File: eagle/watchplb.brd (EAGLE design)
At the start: 100 x 80 mm, 53 parts, among them IC1 SAM-M8Q, IC2 BM70BLES1FC2-0B03AA, Q1 8MHz / LFXTAL020423Reel, U1 MCP111-XXXXX/TO, U2 STM32L073RZ, U3 MCP2200-I/SS

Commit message: update
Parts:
- added C19: CSTCE12M0G15L99-R0, 12mhz osc:CSTCE
- added C20: 1uF, resistor:C0805
- added D1: S8NC-13, diode:SMC
- added J1: (no value), SparkFun-Connectors:USB-B-MICRO-SMD
- added JP2: VIB_MOTOR, 619-28821, pinhead:1X02
- added LED10: YELLOW, adafruit:CHIP-LED0805
- added LED11, LED6, LED7, LED8: GREEN, adafruit:CHIP-LED0805
- added LED12, LED9: RED, adafruit:CHIP-LED0805
- added Q2: DMT5015LFDF, Hick:U-DFN2020-6_TYPE_F
- added R18, R19, R20, R21, R22, R23, R24: 220R, resistor:M0805
- added R25: 100k, resistor:M0805
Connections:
- net N$10 renamed IND_LED_B
- net N$15 renamed IND_LED_W
- net N$17 renamed IND_LED_R
- net N$8 renamed IND_LED_G
- removed net VDD: U3.1
- removed net VSS: U3.20
- removed net VUSB: U3.17
- new net +5V: J1.VBUS, U3.1
- new net N$10: C19.3, U3.3
- new net N$13: LED9.A, R21.2
- new net N$15: C19.1, U3.2
- new net N$17: J1.D-, U3.18
- new net N$19: LED6.A, R18.2
- new net N$20: J1.D+, U3.19
- new net N$21: C20.1, U3.17
- new net N$22: LED7.A, R19.2
- new net N$23: LED12.A, R24.2
- new net N$24: LED10.A, R22.2
- new net N$25: LED8.A, R20.2
- new net N$26: LED11.C, U3.6
- new net N$27: LED12.C, U3.5
- new net N$28: D1.A, JP2.2, Q2.1, Q2.2, Q2.5, Q2.6, Q2.7
- new net N$8: LED11.A, R23.2
- new net POW_LED_G1: R20.1, U2.24
- new net POW_LED_G2: R19.1, U2.25
- new net POW_LED_G3: R18.1, U2.26
- new net POW_LED_R: R21.1, U2.22
- new net POW_LED_Y: R22.1, U2.23
- new net SWD_RX: U3.12
- new net SWD_RXD: U2.16
- new net SWD_TX: U3.10
- new net SWD_TXD: U2.17
- new net V+: D1.C, JP2.1
- new net VIBRATOR: Q2.3, R25.1, U2.44
- net +3V3: now also R23.1, R24.1, U3.4
- net GND: now also C19.2, C20.2, J1.GND, J1.SHIELD1, J1.SHIELD2, J1.SHIELD3, LED10.C, LED6.C, LED7.C, LED8.C, LED9.C, Q2.4, Q2.8, R25.2, U3.20
- net GPS_RXD: now also U2.51; no longer U2.16
- net GPS_TXD: now also U2.52; no longer U2.17

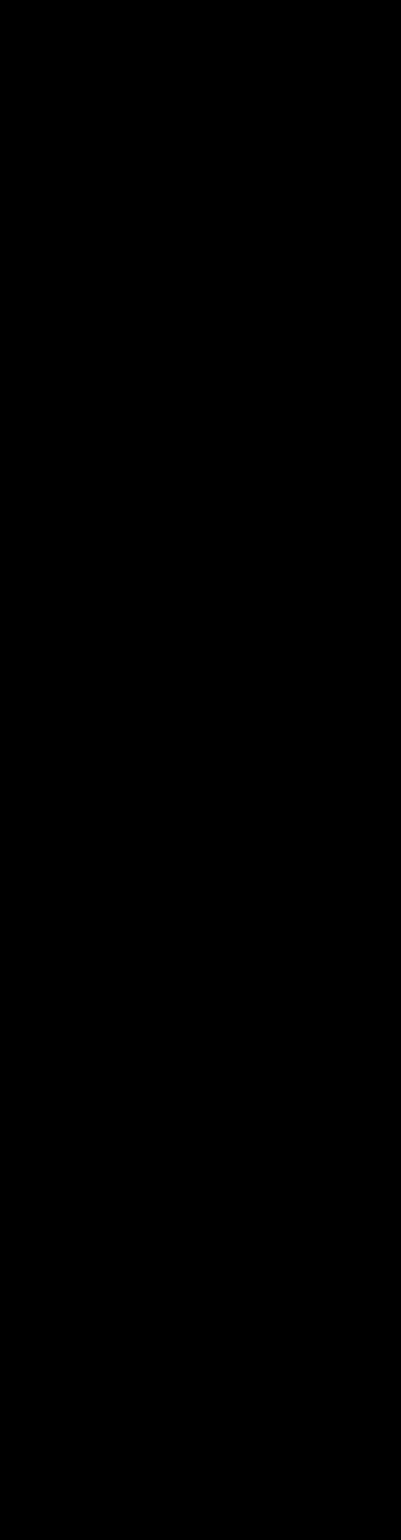
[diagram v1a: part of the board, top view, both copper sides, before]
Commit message: added testpoints, moved pins so pb11 is free to make it pin kompatibel to another prozessor with more power
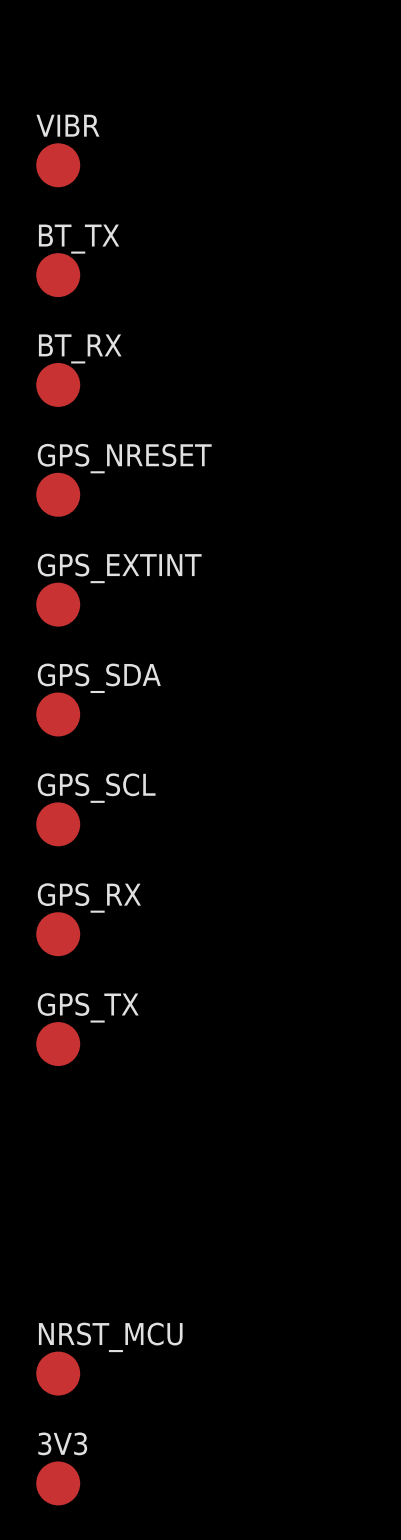
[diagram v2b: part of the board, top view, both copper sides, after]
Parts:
- added 3V3, BT_RX, BT_TX, GPS_EXTINT, GPS_NRESET, GPS_RX, GPS_SCL, GPS_SDA, GPS_TX, NRST_MCU, VIBR: PTR1B2,54, testpad:B2,54
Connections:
- new net RESERVED: U2.30
- net +3V3: now also 3V3.TP
- net BT_HCI_RXD: now also BT_RX.TP
- net BT_HCI_TXD: now also BT_TX.TP
- net GPS_EXTINT: now also GPS_EXTINT.TP
- net GPS_NRESET: now also GPS_NRESET.TP
- net GPS_RXD: now also GPS_RX.TP
- net GPS_SCL: now also GPS_SCL.TP
- net GPS_SDA: now also GPS_SDA.TP
- net GPS_TXD: now also GPS_TX.TP
- net IND_LED_B: now also U2.27; no longer U2.29
- net IND_LED_G: now also U2.28; no longer U2.30
- net IND_LED_R: now also U2.25; no longer U2.27
- net IND_LED_W: now also U2.26; no longer U2.28
- net NRST: now also NRST_MCU.TP
- net POW_LED_G1: now also U2.22; no longer U2.24
- net POW_LED_G2: now also U2.23; no longer U2.25
- net POW_LED_G3: now also U2.24; no longer U2.26
- net POW_LED_R: now also U2.20; no longer U2.22
- net POW_LED_Y: now also U2.21; no longer U2.23
- net VIBRATOR: now also VIBR.TP

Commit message: no message
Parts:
- added SWD_RXD, SWD_TXD, USB_5V, USB_D+, USB_D-: PTR1B2,54, testpad:B2,54
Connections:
- net +5V: now also USB_5V.TP
- net N$17: now also USB_D-.TP
- net N$20: now also USB_D+.TP
- net SWD_RXD: now also SWD_RXD.TP
- net SWD_TXD: now also SWD_TXD.TP
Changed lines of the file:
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@@
 <attribute name="TP_SIGNAL_NAME" value="" x="-121.92" y="-521.97" size="1.778" layer="27" display="off"/>
+</element>
+<element name="USB_D-" library="testpad" package="B2,54" value="PTR1B2,54" x="-121.92" y="-528.32">
+<attribute name="TP_SIGNAL_NAME" value="" x="-121.92" y="-528.32" size="1.778" layer="27" display="off"/>
+</element>
+<element name="USB_D+" library="testpad" package="B2,54" value="PTR1B2,54" x="-121.92" y="-534.67">
+<attribute name="TP_SIGNAL_NAME" value="" x="-121.92" y="-534.67" size="1.778" layer="27" display="off"/>
+</element>
+<element name="USB_5V" library="testpad" package="B2,54" value="PTR1B2,54" x="-121.92" y="-541.02">
+<attribute name="TP_SIGNAL_NAME" value="" x="-121.92" y="-541.02" size="1.778" layer="27" display="off"/>
+</element>
+<element name="SWD_TXD" library="testpad" package="B2,54" value="PTR1B2,54" x="-121.92" y="-547.37">
+<attribute name="TP_SIGNAL_NAME" value="" x="-121.92" y="-547.37" size="1.778" layer="27" display="off"/>
+</element>
+<element name="SWD_RXD" library="testpad" package="B2,54" value="PTR1B2,54" x="-121.92" y="-553.72">
+<attribute name="TP_SIGNAL_NAME" value="" x="-121.92" y="-553.72" size="1.778" layer="27" display="off"/>
 </element>
 </elements>
@@
 <contactref element="J1" pad="D-"/>
 <contactref element="U3" pad="18"/>
+<contactref element="USB_D-" pad="TP"/>
 <wire x1="-81.3816" y1="-262.5344" x2="-98.875" y2="-353.68" width="0" layer="19" extent="1-1"/>
+<wire x1="-121.92" y1="-528.32" x2="-98.875" y2="-353.68" width="0" layer="19" extent="1-1"/>
 </signal>
 <signal name="N$20">
 <contactref element="U3" pad="19"/>
 <contactref element="J1" pad="D+"/>
+<contactref element="USB_D+" pad="TP"/>
 <wire x1="-81.3816" y1="-261.884159375" x2="-98.875" y2="-354.33" width="0" layer="19" extent="1-1"/>
+<wire x1="-121.92" y1="-534.67" x2="-98.875" y2="-354.33" width="0" layer="19" extent="1-1"/>
 </signal>
 <signal name="N$21">
@@
 <contactref element="J1" pad="VBUS"/>
 <contactref element="U3" pad="1"/>
+<contactref element="USB_5V" pad="TP"/>
 <wire x1="-88.7984" y1="-261.23391875" x2="-98.875" y2="-353.03" width="0" layer="19" extent="1-1"/>
+<wire x1="-121.92" y1="-541.02" x2="-98.875" y2="-353.03" width="0" layer="19" extent="1-1"/>
 </signal>
 <signal name="SWD_RX">
@@
 <signal name="SWD_RXD">
 <contactref element="U2" pad="16"/>
+<contactref element="SWD_RXD" pad="TP"/>
+<wire x1="-52.74" y1="-46.93" x2="-121.92" y2="-553.72" width="0" layer="19" extent="1-1"/>
 </signal>
 <signal name="SWD_TXD">
 <contactref element="U2" pad="17"/>
+<contactref element="SWD_TXD" pad="TP"/>
+<wire x1="-50.74" y1="-48.93" x2="-121.92" y2="-547.37" width="0" layer="19" extent="1-1"/>
 </signal>
 <signal name="N$28">

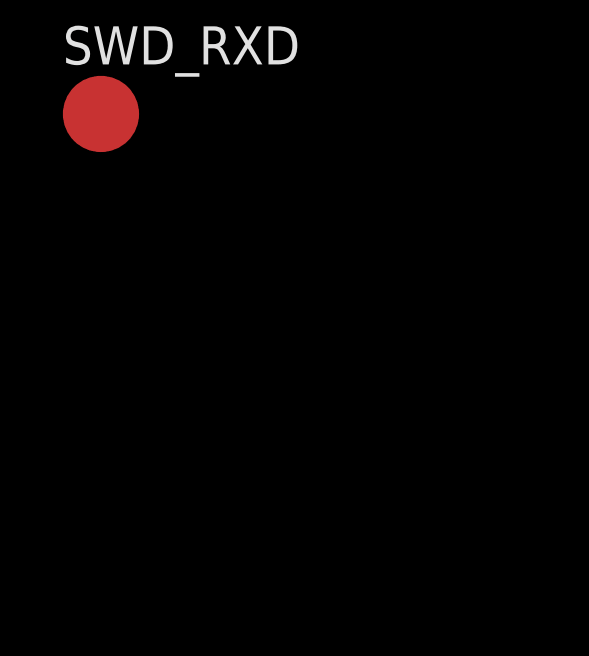
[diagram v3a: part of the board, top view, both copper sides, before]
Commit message: added wakeup pin support and page for psu (empty atm)
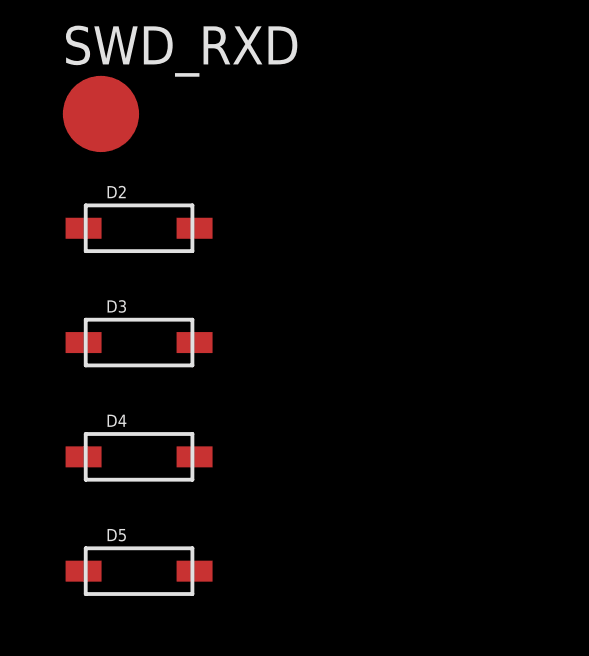
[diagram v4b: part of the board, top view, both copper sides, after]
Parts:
- added D2, D3, D4, D5: (no value), adafruit:SOD-123
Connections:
- new net MCU_WAKEUP: D2.C, D3.C, D4.C, D5.C, U2.14
- net BTN_1: now also D2.A
- net BTN_2: now also D3.A
- net BTN_3: now also D4.A
- net BTN_4: now also D5.A
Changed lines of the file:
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@@
 <attribute name="TP_SIGNAL_NAME" value="" x="-121.92" y="-553.72" size="1.778" layer="27" display="off"/>
 </element>
+<element name="D2" library="adafruit" package="SOD-123" value="" x="-120.65" y="-557.53"/>
+<element name="D3" library="adafruit" package="SOD-123" value="" x="-120.65" y="-561.34"/>
+<element name="D4" library="adafruit" package="SOD-123" value="" x="-120.65" y="-565.15"/>
+<element name="D5" library="adafruit" package="SOD-123" value="" x="-120.65" y="-568.96"/>
 </elements>
 <signals>
@@
 <contactref element="S3" pad="4"/>
 <contactref element="U2" pad="38"/>
+<contactref element="D3" pad="A"/>
 <wire x1="-75.6412" y1="-140.6906" x2="-75.88" y2="-151.13" width="0" layer="19" extent="1-1"/>
 <wire x1="-69.1388" y1="-140.6906" x2="-75.6412" y2="-140.6906" width="0" layer="19" extent="1-1"/>
 <wire x1="-66.36" y1="-144.78" x2="-69.1388" y2="-140.6906" width="0" layer="19" extent="1-1"/>
 <wire x1="-41.24" y1="-44.43" x2="-69.1388" y2="-140.6906" width="0" layer="19" extent="1-1"/>
+<wire x1="-118.8" y1="-561.34" x2="-75.88" y2="-151.13" width="0" layer="19" extent="1-1"/>
 </signal>
 <signal name="N$7">
@@
 <contactref element="S2" pad="4"/>
 <contactref element="U2" pad="33"/>
+<contactref element="D2" pad="A"/>
 <wire x1="-73.98" y1="-116.84" x2="-75.88" y2="-123.19" width="0" layer="19" extent="1-1"/>
 <wire x1="-75.6412" y1="-102.5906" x2="-73.98" y2="-116.84" width="0" layer="19" extent="1-1"/>
 <wire x1="-69.1388" y1="-102.5906" x2="-75.6412" y2="-102.5906" width="0" layer="19" extent="1-1"/>
 <wire x1="-41.24" y1="-46.93" x2="-69.1388" y2="-102.5906" width="0" layer="19" extent="1-1"/>
+<wire x1="-118.8" y1="-557.53" x2="-75.88" y2="-123.19" width="0" layer="19" extent="1-1"/>
 </signal>
 <signal name="N$5">
@@
 <contactref element="S4" pad="4"/>
 <contactref element="U2" pad="39"/>
-<wire x1="-81.8388" y1="-216.8906" x2="-41.24" y2="-43.93" width="0" layer="19" extent="1-1"/>
+<contactref element="D4" pad="A"/>
+<wire x1="-88.58" y1="-227.33" x2="-118.8" y2="-565.15" width="0" layer="19" extent="1-1"/>
+<wire x1="-88.3412" y1="-216.8906" x2="-88.58" y2="-227.33" width="0" layer="19" extent="1-1"/>
+<wire x1="-81.8388" y1="-216.8906" x2="-88.3412" y2="-216.8906" width="0" layer="19" extent="1-1"/>
 <wire x1="-79.06" y1="-220.98" x2="-81.8388" y2="-216.8906" width="0" layer="19" extent="1-1"/>
-<wire x1="-88.3412" y1="-216.8906" x2="-81.8388" y2="-216.8906" width="0" layer="19" extent="1-1"/>
-<wire x1="-88.58" y1="-227.33" x2="-88.3412" y2="-216.8906" width="0" layer="19" extent="1-1"/>
+<wire x1="-41.24" y1="-43.93" x2="-81.8388" y2="-216.8906" width="0" layer="19" extent="1-1"/>
 </signal>
 <signal name="N$14">
@@
 <contactref element="S5" pad="4"/>
 <contactref element="U2" pad="40"/>
+<contactref element="D5" pad="A"/>
+<wire x1="-88.58" y1="-287.02" x2="-118.8" y2="-568.96" width="0" layer="19" extent="1-1"/>
 <wire x1="-88.3412" y1="-276.5806" x2="-88.58" y2="-287.02" width="0" layer="19" extent="1-1"/>
 <wire x1="-81.8388" y1="-276.5806" x2="-88.3412" y2="-276.5806" width="0" layer="19" extent="1-1"/>
@@
 <contactref element="U2" pad="30"/>
 </signal>
+<signal name="MCU_WAKEUP">
+<contactref element="U2" pad="14"/>
+<contactref element="D5" pad="C"/>
+<contactref element="D2" pad="C"/>
+<contactref element="D3" pad="C"/>
+<contactref element="D4" pad="C"/>
+<wire x1="-122.5" y1="-565.15" x2="-122.5" y2="-568.96" width="0" layer="19" extent="1-1"/>
+<wire x1="-122.5" y1="-561.34" x2="-122.5" y2="-565.15" width="0" layer="19" extent="1-1"/>
+<wire x1="-122.5" y1="-557.53" x2="-122.5" y2="-561.34" width="0" layer="19" extent="1-1"/>
+<wire x1="-52.74" y1="-45.93" x2="-122.5" y2="-557.53" width="0" layer="19" extent="1-1"/>
+</signal>
 </signals>

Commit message: added mouser numbers for most products, changed switches to smd
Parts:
- added BTN_1, BTN_2, BTN_3, BTN_4, BTN_NRST: PTR1B2,54, testpad:B2,54
- LED1: value (none) -> BLUE
- S1, S2, S3, S4, S5: device switch-omron:B3F-10XX -> Hick:SMD_SWITCH
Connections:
- net +3V3: now also S2.P$3, S2.P$4, S3.P$3, S3.P$4, S4.P$3, S4.P$4, S5.P$3, S5.P$4; no longer S2.1, S2.2, S3.1, S3.2, S4.1, S4.2, S5.1, S5.2
- net BTN_1: now also BTN_1.TP, S2.P$1, S2.P$2; no longer S2.3, S2.4
- net BTN_2: now also BTN_2.TP, S3.P$1, S3.P$2; no longer S3.3, S3.4
- net BTN_3: now also BTN_3.TP, S4.P$1, S4.P$2; no longer S4.3, S4.4
- net BTN_4: now also BTN_4.TP, S5.P$1, S5.P$2; no longer S5.3, S5.4
- net GND: now also S1.P$1, S1.P$2; no longer S1.3, S1.4
- net NRST: now also BTN_NRST.TP, S1.P$3, S1.P$4; no longer S1.1, S1.2

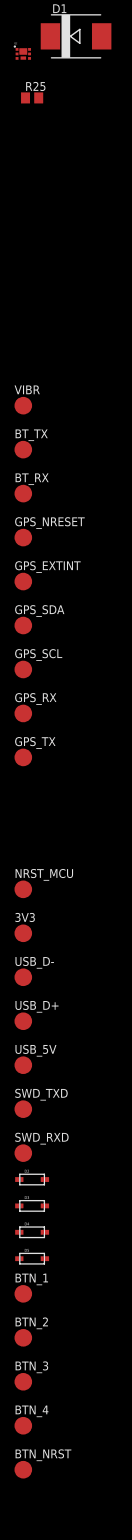
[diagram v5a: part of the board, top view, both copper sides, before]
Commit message: changed mosfet to one with sot23 footprint
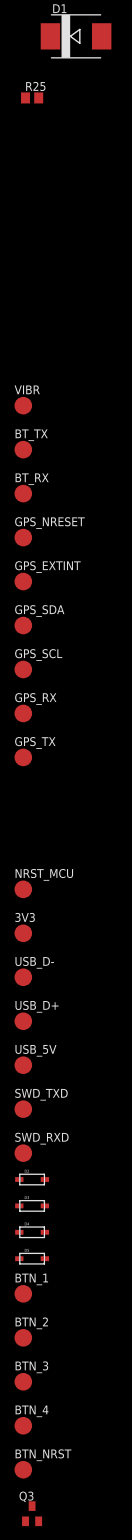
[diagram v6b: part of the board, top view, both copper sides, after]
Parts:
- removed Q2: DMT5015LFDF, Hick:U-DFN2020-6_TYPE_F
- added Q3: DMN3023L-7, transistor-small-signal:SOT23
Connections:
- net GND: now also Q3.2; no longer Q2.4, Q2.8
- net N$28: now also Q3.3; no longer Q2.1, Q2.2, Q2.5, Q2.6, Q2.7
- net VIBRATOR: now also Q3.1; no longer Q2.3
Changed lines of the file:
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@@
 <element name="JP2" library="pinhead" package="1X02" value="VIB_MOTOR, 619-28821" x="-115.57" y="-383.54"/>
 <element name="D1" library="diode" package="SMC" value="S8NC-13 " x="-114.3" y="-392.43"/>
-<element name="Q2" library="Hick" package="U-DFN2020-6_TYPE_F" value="DMT5015LFDF" x="-121.92" y="-394.97"/>
 <element name="R25" library="resistor" package="M0805" value="100k" x="-120.65" y="-401.32"/>
 <element name="VIBR" library="testpad" package="B2,54" value="PTR1B2,54" x="-121.92" y="-445.77">
@@
 <attribute name="TP_SIGNAL_NAME" value="" x="-121.92" y="-599.44" size="1.778" layer="27" display="off"/>
 </element>
+<element name="Q3" library="transistor-small-signal" package="SOT23" value="DMN3023L-7 " x="-120.65" y="-605.79"/>
 </elements>
 <signals>
@@
 <contactref element="J1" pad="SHIELD1"/>
 <contactref element="J1" pad="SHIELD2"/>
-<contactref element="Q2" pad="8"/>
-<contactref element="Q2" pad="4"/>
 <contactref element="R25" pad="2"/>
+<contactref element="Q3" pad="2"/>
 <wire x1="-74.08" y1="-166.37" x2="-74.08" y2="-172.72" width="0" layer="19" extent="1-1"/>
 <wire x1="-74.93" y1="-185.42" x2="-74.08" y2="-172.72" width="0" layer="19" extent="1-1"/>
@@
 <wire x1="-73.98" y1="-123.19" x2="-75.78" y2="-129.54" width="0" layer="19" extent="1-1"/>
 <wire x1="-64.35" y1="-97.79" x2="-73.98" y2="-123.19" width="0" layer="19" extent="1-1"/>
-<wire x1="-56.96" y1="-86.13" x2="-64.35" y2="-97.79" width="0" layer="19" extent="1-1"/>
-<wire x1="-64.96" y1="-89.13" x2="-56.96" y2="-86.13" width="0" layer="19" extent="1-1"/>
-<wire x1="-52.92" y1="-91.44" x2="-64.96" y2="-89.13" width="0" layer="19" extent="1-1"/>
-<wire x1="-50.67" y1="-85.09" x2="-52.92" y2="-91.44" width="0" layer="19" extent="1-1"/>
+<wire x1="-64.96" y1="-89.13" x2="-64.35" y2="-97.79" width="0" layer="19" extent="1-1"/>
+<wire x1="-56.96" y1="-86.13" x2="-64.96" y2="-89.13" width="0" layer="19" extent="1-1"/>
+<wire x1="-50.67" y1="-85.09" x2="-56.96" y2="-86.13" width="0" layer="19" extent="1-1"/>
 <wire x1="-51.22" y1="-78.74" x2="-50.67" y2="-85.09" width="0" layer="19" extent="1-1"/>
 <wire x1="-51.22" y1="-72.39" x2="-51.22" y2="-78.74" width="0" layer="19" extent="1-1"/>
@@
 <wire x1="-52.74" y1="-44.93" x2="-50.24" y2="-48.93" width="0" layer="19" extent="1-1"/>
 <wire x1="-43.74" y1="-48.93" x2="-50.24" y2="-48.93" width="0" layer="19" extent="1-1"/>
+<wire x1="-52.92" y1="-91.44" x2="-56.96" y2="-86.13" width="0" layer="19" extent="1-1"/>
 <wire x1="-50.24" y1="-37.43" x2="-52.74" y2="-44.93" width="0" layer="19" extent="1-1"/>
 <wire x1="-48.74" y1="-37.43" x2="-50.24" y2="-37.43" width="0" layer="19" extent="1-1"/>
@@
 <wire x1="-103.29" y1="-364.49" x2="-101.6" y2="-358.015" width="0" layer="19" extent="1-1"/>
 <wire x1="-92.71" y1="-359.41" x2="-98.875" y2="-355.63" width="0" layer="19" extent="1-1"/>
-<wire x1="-121.02" y1="-395.62" x2="-103.29" y2="-364.49" width="0" layer="19" extent="1-1"/>
-<wire x1="-121.92" y1="-395.57" x2="-121.02" y2="-395.62" width="0" layer="19" extent="1-1"/>
-<wire x1="-119.7" y1="-401.32" x2="-121.02" y2="-395.62" width="0" layer="19" extent="1-1"/>
+<wire x1="-119.7" y1="-401.32" x2="-103.29" y2="-364.49" width="0" layer="19" extent="1-1"/>
 <wire x1="1.66" y1="36.51" x2="-25.82" y2="-3.81" width="0" layer="19" extent="1-1"/>
 <wire x1="2.76" y1="36.51" x2="1.66" y2="36.51" width="0" layer="19" extent="1-1"/>
@@
 <wire x1="41.66" y1="40.65" x2="41.66" y2="48.25" width="0" layer="19" extent="16-16"/>
 <wire x1="44.46" y1="37.85" x2="41.66" y2="40.65" width="0" layer="19" extent="16-16"/>
+<wire x1="-119.7" y1="-606.89" x2="-119.7" y2="-401.32" width="0" layer="19" extent="1-1"/>
 </signal>
 <signal name="BT_NRST">
@@
 <contactref element="JP2" pad="2"/>
 <contactref element="D1" pad="A"/>
-<contactref element="Q2" pad="1"/>
-<contactref element="Q2" pad="5"/>
-<contactref element="Q2" pad="6"/>
-<contactref element="Q2" pad="2"/>
-<contactref element="Q2" pad="7"/>
+<contactref element="Q3" pad="3"/>
 <wire x1="-114.3" y1="-383.54" x2="-110.6" y2="-392.43" width="0" layer="19" extent="1-1"/>
-<wire x1="-121.02" y1="-394.32" x2="-110.6" y2="-392.43" width="0" layer="19" extent="1-1"/>
-<wire x1="-121.02" y1="-394.97" x2="-121.02" y2="-394.32" width="0" layer="19" extent="1-1"/>
-<wire x1="-121.92" y1="-394.62" x2="-121.02" y2="-394.32" width="0" layer="19" extent="1-1"/>
-<wire x1="-122.82" y1="-394.32" x2="-121.92" y2="-394.62" width="0" layer="19" extent="1-1"/>
-<wire x1="-122.82" y1="-394.97" x2="-122.82" y2="-394.32" width="0" layer="19" extent="1-1"/>
+<wire x1="-120.65" y1="-604.69" x2="-110.6" y2="-392.43" width="0" layer="19" extent="1-1"/>
 </signal>
 <signal name="V+">
@@
 </signal>
 <signal name="VIBRATOR">
-<contactref element="Q2" pad="3"/>
 <contactref element="R25" pad="1"/>
 <contactref element="U2" pad="44"/>
 <contactref element="VIBR" pad="TP"/>
-<wire x1="-122.82" y1="-395.62" x2="-41.24" y2="-41.43" width="0" layer="19" extent="1-1"/>
-<wire x1="-121.6" y1="-401.32" x2="-122.82" y2="-395.62" width="0" layer="19" extent="1-1"/>
-<wire x1="-121.92" y1="-445.77" x2="-121.6" y2="-401.32" width="0" layer="19" extent="1-1"/>
+<contactref element="Q3" pad="1"/>
+<wire x1="-121.92" y1="-445.77" x2="-121.6" y2="-606.89" width="0" layer="19" extent="1-1"/>
+<wire x1="-121.6" y1="-401.32" x2="-121.92" y2="-445.77" width="0" layer="19" extent="1-1"/>
+<wire x1="-41.24" y1="-41.43" x2="-121.6" y2="-401.32" width="0" layer="19" extent="1-1"/>
 </signal>
 <signal name="RESERVED">
